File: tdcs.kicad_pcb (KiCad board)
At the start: 2 copper layers, 50 x 30 mm, 0 parts

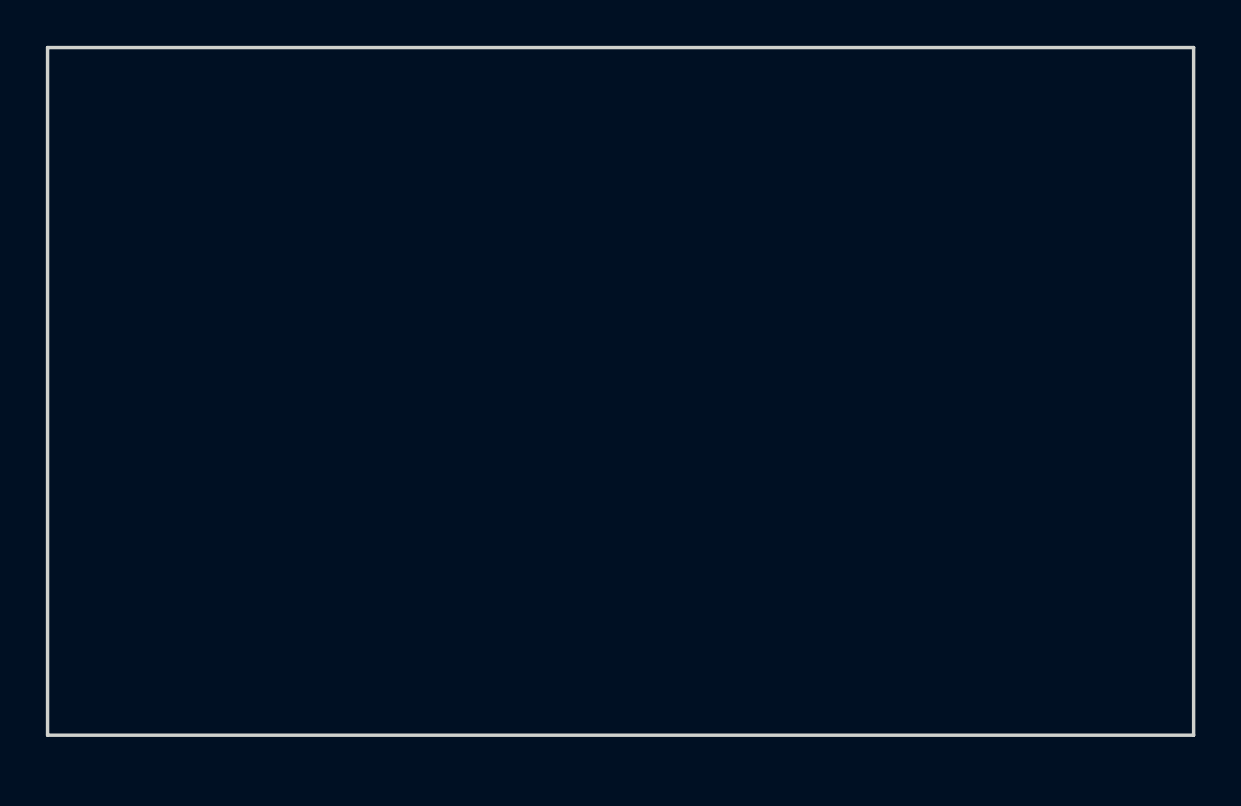
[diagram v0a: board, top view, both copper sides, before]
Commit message: Complete PCB layout with all components placed and routed
2-layer board, all 18 THT components placed and traces routed.
DRC passes clean.
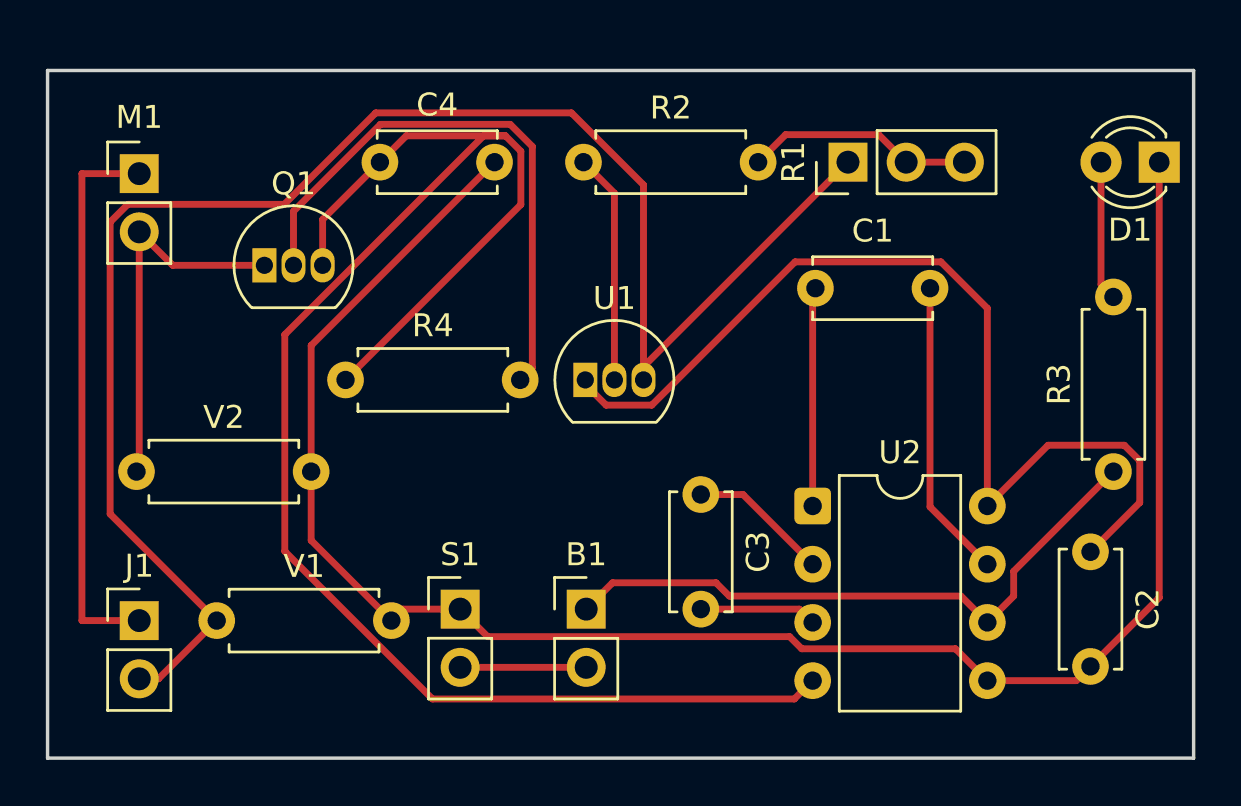
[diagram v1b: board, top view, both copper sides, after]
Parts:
- added B1: 9V, Connector_PinHeader_2.54mm:PinHeader_1x02_P2.54mm_Vertical, F.Cu at (43.5, 44.5)
- added C1: 10uF, Capacitor_THT:C_Disc_D5.0mm_W2.5mm_P5.00mm, F.Cu at (53.5, 30.5)
- added C2: 10uF, Capacitor_THT:C_Disc_D5.0mm_W2.5mm_P5.00mm, F.Cu at (65.5, 42.0)
- added C3: 10uF, Capacitor_THT:C_Disc_D5.0mm_W2.5mm_P5.00mm, F.Cu at (48.5, 39.5)
- added C4: 10uF, Capacitor_THT:C_Disc_D5.0mm_W2.5mm_P5.00mm, F.Cu at (34.5, 25.0)
- added D1: LED, LED_THT:LED_D3.0mm, F.Cu at (68.5, 25.0)
- added J1: Electrodes, Connector_PinHeader_2.54mm:PinHeader_1x02_P2.54mm_Vertical, F.Cu at (24.0, 45.0)
- added M1: 0-2.0mA, Connector_PinHeader_2.54mm:PinHeader_1x02_P2.54mm_Vertical, F.Cu at (24.0, 25.5)
- added Q1: MMBFJ111, Package_TO_SOT_THT:TO-92_Inline, F.Cu at (29.5, 29.5)
- added R1: 0-100, Connector_PinHeader_2.54mm:PinHeader_1x03_P2.54mm_Vertical, F.Cu at (54.9, 25.0)
- added R2: 30, Resistor_THT:R_Axial_DIN0207_L6.3mm_D2.5mm_P7.62mm_Horizontal, F.Cu at (43.4, 25.0)
- added R3: 806, Resistor_THT:R_Axial_DIN0207_L6.3mm_D2.5mm_P7.62mm_Horizontal, F.Cu at (66.5, 38.5)
- added R4: 806, Resistor_THT:R_Axial_DIN0207_L6.3mm_D2.5mm_P7.62mm_Horizontal, F.Cu at (33.0, 34.5)
- added S1: SW_SPST, Connector_PinHeader_2.54mm:PinHeader_1x02_P2.54mm_Vertical, F.Cu at (38.0, 44.5)
- added U1: LM334Z, Package_TO_SOT_THT:TO-92_Inline, F.Cu at (43.5, 34.5)
- added U2: LT1026, Package_DIP:DIP-8_W7.62mm, F.Cu at (53.4, 40.0)
- added V1: V68MA3B, Resistor_THT:R_Axial_DIN0207_L6.3mm_D2.5mm_P7.62mm_Horizontal, F.Cu at (27.4, 45.0)
- added V2: V68MA3B, Resistor_THT:R_Axial_DIN0207_L6.3mm_D2.5mm_P7.62mm_Horizontal, F.Cu at (23.9, 38.5)
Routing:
- net GND: track 0.00 -> 80.3 mm
- net Net-(Q1-G): track 0.00 -> 74.3 mm
- net Net-(J1-Pin_2): track 0.00 -> 72.0 mm
- net Net-(U2-+Vout): track 0.00 -> 43.1 mm
- net VCC: track 0.00 -> 27.6 mm
- net Net-(Q1-S): track 0.00 -> 25.2 mm
- net Net-(J1-Pin_1): track 0.00 -> 24.5 mm
- net Net-(M1-+): track 0.00 -> 16.6 mm
- net Net-(U2-C1+): track 0.00 -> 13.1 mm
- net Net-(R2-Pad1): track 0.00 -> 10.1 mm
- net Net-(R1-Pad2): track 0.00 -> 9.99 mm
- net Net-(U2-C1-): track 0.00 -> 9.55 mm
- net Net-(U2-C2+): track 0.00 -> 6.14 mm
- net Net-(D1-A): track 0.00 -> 6.10 mm
- net Net-(B1--): track 0.00 -> 5.50 mm
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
